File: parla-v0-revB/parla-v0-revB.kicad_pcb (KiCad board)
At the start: 2 copper layers, 70 x 70 mm, 0 parts

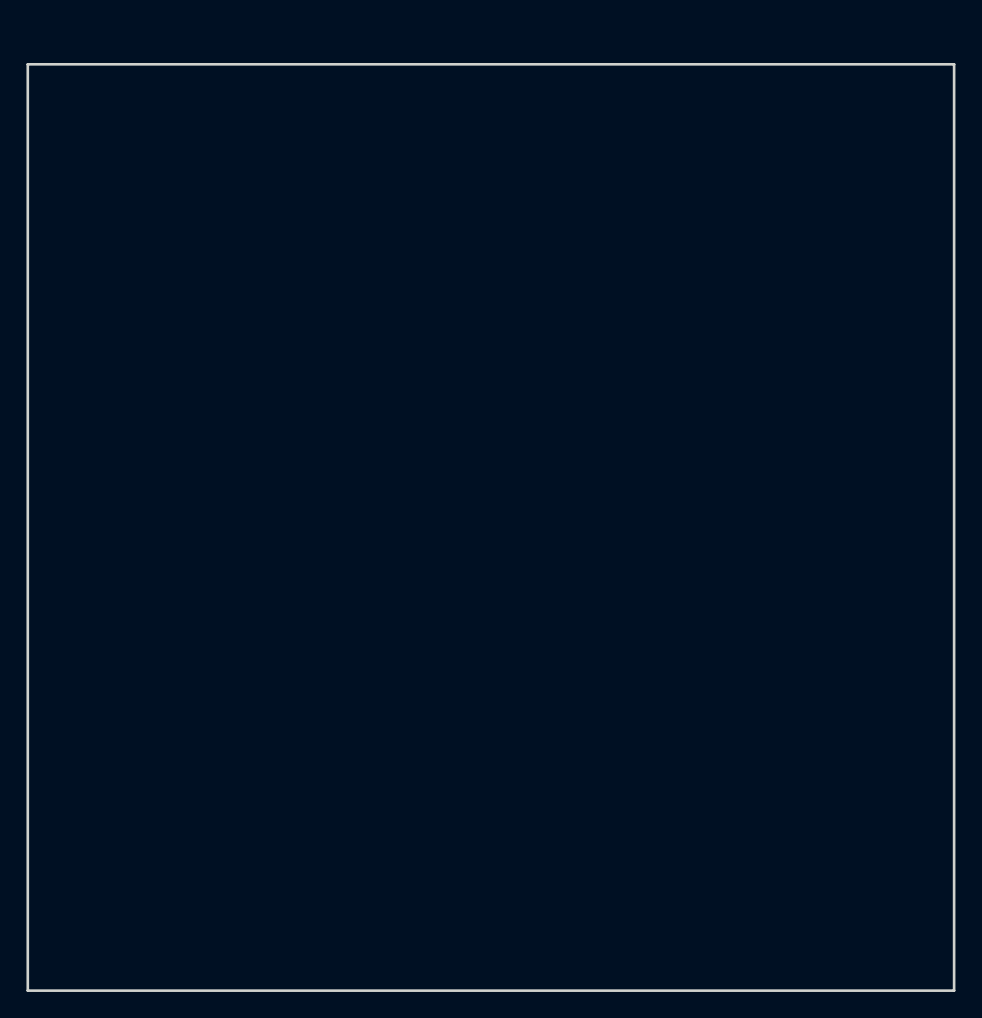
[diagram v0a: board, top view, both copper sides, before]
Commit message: actualizada version smd
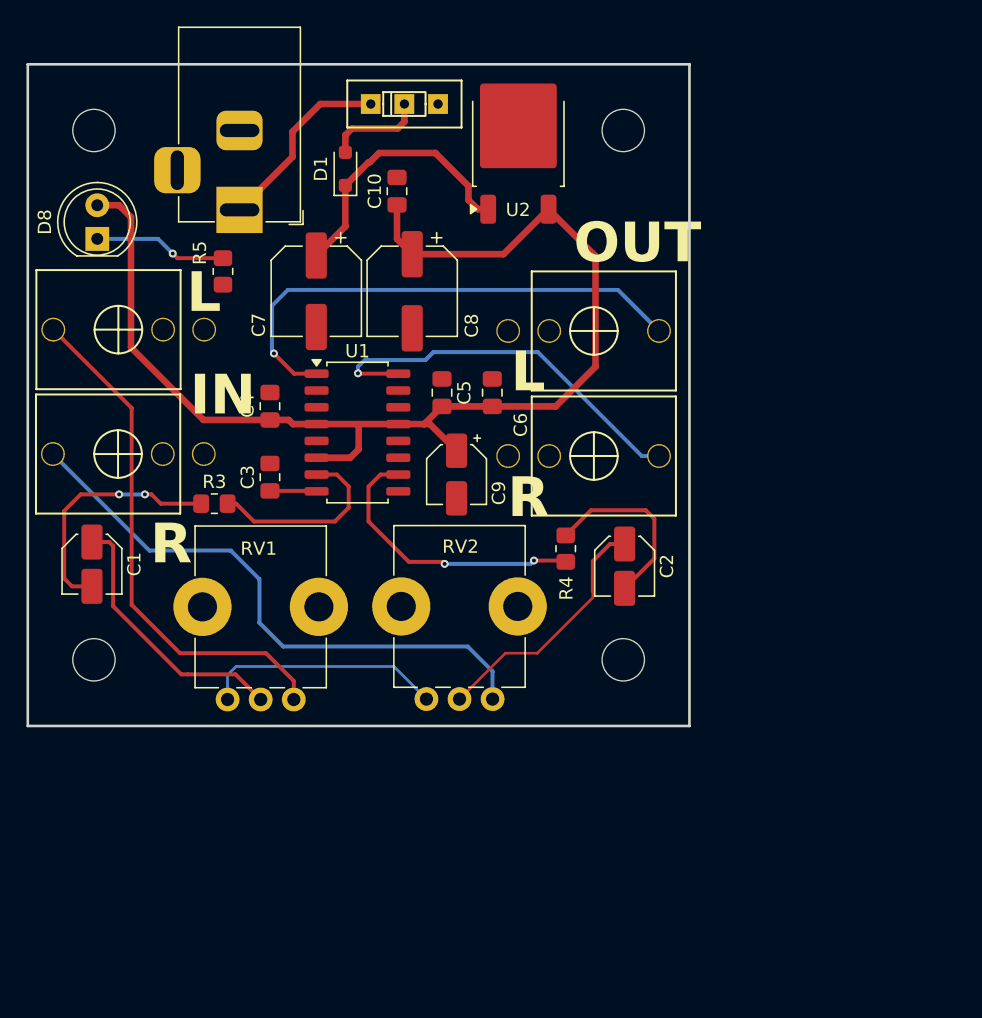
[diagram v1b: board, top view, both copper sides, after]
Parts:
- added C1: 470n, Capacitor_SMD:C_Elec_4x5.4, F.Cu at (54.9, 87.8)
- added C10: 100n, Capacitor_SMD:C_0805_2012Metric_Pad1.18x1.45mm_HandSolder, F.Cu at (77.9, 59.6)
- added C2: 470n, Capacitor_SMD:C_Elec_4x5.4, F.Cu at (95.1, 87.9)
- added C3: 100n, Capacitor_SMD:C_0805_2012Metric_Pad1.18x1.45mm_HandSolder, F.Cu at (68.3, 81.2)
- added C4: 1u, Capacitor_SMD:C_0805_2012Metric_Pad1.18x1.45mm_HandSolder, F.Cu at (68.3, 75.8)
- added C5: 1u, Capacitor_SMD:C_0805_2012Metric_Pad1.18x1.45mm_HandSolder, F.Cu at (81.3, 74.8)
- added C6: 1u, Capacitor_SMD:C_0805_2012Metric_Pad1.18x1.45mm_HandSolder, F.Cu at (85.1, 74.8)
- added C7: 100u, Capacitor_SMD:CP_Elec_6.3x7.7, F.Cu at (71.8, 67.2)
- added C8: 220u, Capacitor_SMD:CP_Elec_6.3x5.4, F.Cu at (79.0, 67.2)
- added C9: 10u, Capacitor_SMD:CP_Elec_4x5.4, F.Cu at (82.4, 81.0)
- added D1: 1N4007, Diode_SMD:D_SOD-323_HandSoldering, F.Cu at (74.0, 57.9)
- added D8: LED, LED_THT:LED_D5.0mm, F.Cu at (55.2, 63.2)
- added H1: M3, MountingHole:MountingHole_3.2mm_M3, F.Cu at (55.0, 55.0)
- added H2: M3, MountingHole:MountingHole_3.2mm_M3, F.Cu at (95.0, 55.0)
- added H3: M3, MountingHole:MountingHole_3.2mm_M3, F.Cu at (55.0, 95.0)
- added H4: M3, MountingHole:MountingHole_3.2mm_M3, F.Cu at (95.0, 95.0)
- added J1: AudioJack2_SwitchT, dis8644:PJ301M-12-T_TN_S, F.Cu at (92.8, 70.2)
- added J2: AudioJack2_SwitchT, dis8644:PJ301M-12-T_TN_S, F.Cu at (92.8, 79.6)
- added J3: AudioJack2_SwitchT, dis8644:PJ301M-12-T_TN_S, F.Cu at (56.8, 70.0)
- added J4: AudioJack2_SwitchT, dis8644:PJ301M-12-T_TN_S, F.Cu at (56.8, 79.5)
- added J5: Barrel_Jack_Switch, Connector_BarrelJack:BarrelJack_Horizontal, F.Cu at (66.0, 61.0)
- added R3: 10k, Resistor_SMD:R_0805_2012Metric_Pad1.20x1.40mm_HandSolder, F.Cu at (64.1, 83.2)
- added R4: 10k, Resistor_SMD:R_0805_2012Metric_Pad1.20x1.40mm_HandSolder, F.Cu at (90.7, 86.6)
- added R5: 1k, Resistor_SMD:R_0805_2012Metric_Pad1.20x1.40mm_HandSolder, F.Cu at (64.8, 65.7)
- added RV1: 50k, Potentiometer_THT:Potentiometer_Bourns_PTV09A-1_Single_Vertical, F.Cu at (70.1, 98.0)
- added RV2: 50k, Potentiometer_THT:Potentiometer_Bourns_PTV09A-1_Single_Vertical, F.Cu at (85.1, 98.0)
- added SW3: SW_SPDT, dis8644:spdt_ssd12d00g3, F.Cu at (78.5, 53.0)
- added U1: PAM8403D, Package_SO:SOP-16_4.4x10.4mm_P1.27mm, F.Cu at (74.9, 77.8)
- added U2: L7805, Package_TO_SOT_SMD:TO-252-2, F.Cu at (87.1, 55.9)
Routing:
- net +5V: track 0.00 -> 90.0 mm
- net Net-(J4-PadT): track 0.00 -> 44.1 mm
- net Net-(J3-PadT): track 0.00 -> 39.3 mm
- net Net-(U1-LOUT+): track 0.00 -> 38.6 mm, vias 0 -> 1
- net Net-(U1-ROUT+): track 0.00 -> 30.1 mm, vias 0 -> 1
- net Net-(U1-INR): track 0.00 -> 21.6 mm, vias 0 -> 2
- net +12V: track 0.00 -> 20.4 mm
- net Net-(C1-Pad1): track 0.00 -> 20.3 mm
- net Net-(C2-Pad1): track 0.00 -> 18.9 mm
- net Net-(C1-Pad2): track 0.00 -> 18.6 mm, vias 0 -> 2
- net GND: track 0.00 -> 18.2 mm
- net Net-(U1-INL): track 0.00 -> 14.5 mm
- net Net-(SW3-A): track 0.00 -> 14.3 mm
- net Net-(C2-Pad2): track 0.00 -> 13.9 mm
- net Net-(D8-K): track 0.00 -> 10.1 mm, vias 0 -> 1
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- added copper zone on B.Cu, net GND
- added copper zone on F.Cu, net GND
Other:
- board size 70 x 70 mm -> 50 x 50 mm
- board text added: "IN"
- board text added: "L"
- board text added: "OUT"
- board text added: "PARLA"
- board text added: "R"
- board text added: "rev B 06-2026"
